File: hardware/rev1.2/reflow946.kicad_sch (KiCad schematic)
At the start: 56 parts, among them J1 VH-2A, J2 VH-3A2, J3 VH-3A2, J4 XH-A2, J5 HDR-M-2.54_2x3, J6 TFT_1.47, J7 PROBE_BRK, J8 EXT_TC, Q1 BTA16-600BRG, Q2 MMBT3906, Q3 MMBT3906, Q4 MMBT3906, SW1 SW_Push, SW2 SW_Push, SW3 SW_Push, U1 MOC3041M, U2 ESP32-WROOM-32U, U3 MAX31855KASA, U4 AMS1117-3.3, U6 MAX31855KASA

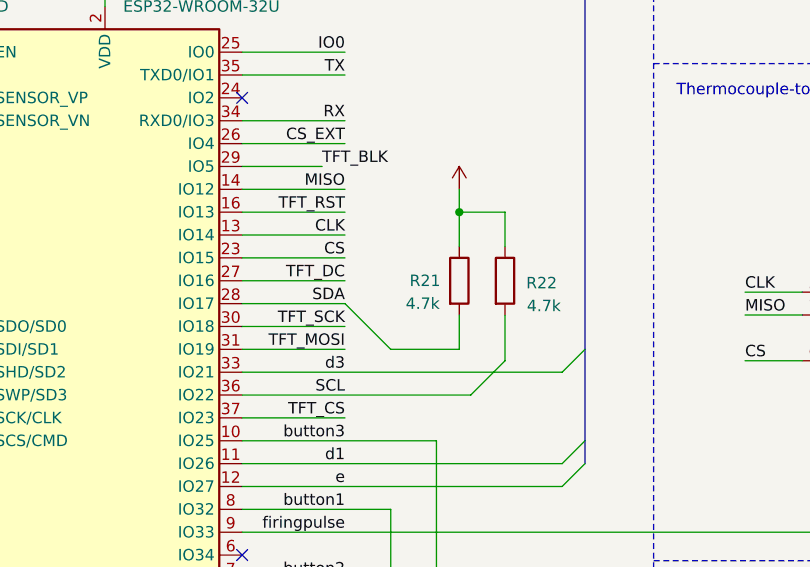
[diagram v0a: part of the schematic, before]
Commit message: rev2: remove I2C expansion pull-ups R21/R22 (vestigial — display went SPI; IO17/IO22 spare)
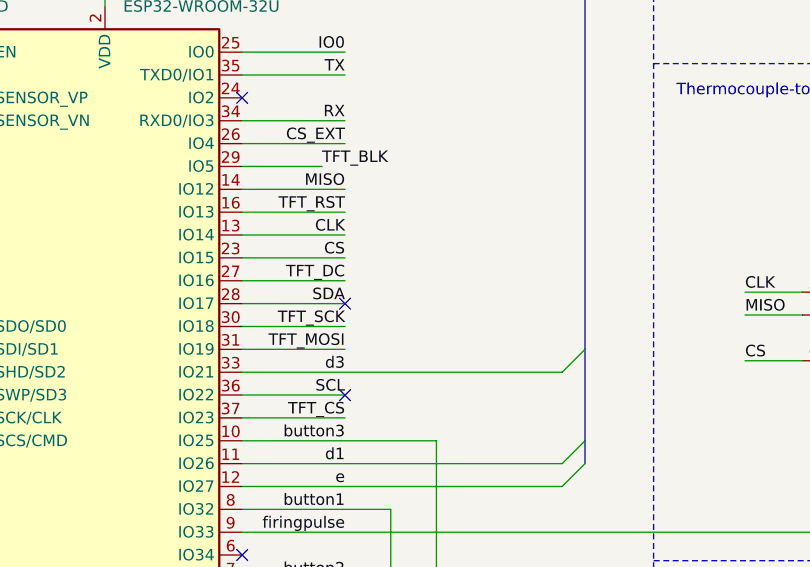
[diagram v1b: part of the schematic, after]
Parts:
- removed R21, R22: 4.7k, Resistor_SMD:R_0603_1608Metric_Pad0.98x0.95mm_HandSolder, symbol Device:R
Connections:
- no-connect marks 17 -> 19

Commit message: schematic: J6 pins reordered to FPC tail order (BL/CS/DC/RES/SDA/SCL/VDD/GND); footprint -> FH12-8S-0.5SH 0.5mm top-contact
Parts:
- J6: footprint Connector_PinHeader_2.54mm:PinHeader_1x08_P2.54mm_Vertical -> Connector_FFC-FPC:Hirose_FH12-8S-0.5SH_1x08-1MP_P0.50mm_Horizontal
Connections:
- net +3.3V: now also J6.7 (Pin_7); no longer J6.1 (Pin_1)
- net GND: now also J6.8 (Pin_8); no longer J6.2 (Pin_2)
- net TFT_BLK: now also J6.1 (Pin_1); no longer J6.8 (Pin_8)
- net TFT_CS: now also J6.2 (Pin_2); no longer J6.3 (Pin_3)
- net TFT_DC: now also J6.3 (Pin_3); no longer J6.4 (Pin_4)
- net TFT_MOSI: now also J6.5 (Pin_5); no longer J6.7 (Pin_7)
- net TFT_RST: now also J6.4 (Pin_4); no longer J6.5 (Pin_5)
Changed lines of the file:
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@@
 	(wire
 		(pts
-			(xy 181.61 223.52) (xy 176.53 223.52)
+			(xy 181.61 223.52) (xy 171.45 223.52)
 		)
 		(stroke
@@
 	(wire
 		(pts
-			(xy 171.45 236.22) (xy 181.61 236.22)
+			(xy 176.53 236.22) (xy 181.61 236.22)
 		)
 		(stroke
@@
 	(wire
 		(pts
-			(xy 181.61 220.98) (xy 176.53 220.98)
+			(xy 181.61 220.98) (xy 171.45 220.98)
 		)
 		(stroke
@@
 	(wire
 		(pts
-			(xy 171.45 238.76) (xy 181.61 238.76)
+			(xy 176.53 238.76) (xy 181.61 238.76)
 		)
 		(stroke
@@
 		)
 	)
-	(label "TFT_DC"
+	(label "TFT_RST"
 		(at 171.45 228.6 180)
 		(effects
@@
 		)
 	)
-	(label "TFT_CS"
+	(label "TFT_DC"
 		(at 171.45 226.06 180)
 		(effects
@@
 		)
 	)
-	(label "TFT_RST"
+	(label "TFT_MOSI"
 		(at 171.45 231.14 180)
 		(effects
@@
 		)
 	)
-	(label "TFT_MOSI"
-		(at 171.45 236.22 180)
-		(effects
-			(font
-				(size 1.27 1.27)
-			)
-			(justify right bottom)
-		)
-	)
 	(label "RX"
 		(at 120.65 231.14 0)
@@
 	)
 	(label "TFT_BLK"
-		(at 171.45 238.76 180)
+		(at 171.45 220.98 180)
+		(effects
+			(font
+				(size 1.27 1.27)
+			)
+			(justify right bottom)
+		)
+	)
+	(label "TFT_CS"
+		(at 171.45 223.52 180)
 		(effects
 			(font
@@
 	)
 	(symbol
+		(lib_id "power:GND")
+		(at 176.53 238.76 0)
+		(unit 1)
+		(body_style 1)
+		(exclude_from_sim no)
+		(in_bom yes)
+		(on_board yes)
+		(in_pos_files yes)
+		(dnp no)
+		(fields_autoplaced yes)
+		(property "Reference" "#PWR0126"
+			(at 176.53 242.57 0)
+			(hide yes)
+			(show_name no)
+			(do_not_autoplace no)
+			(effects
+				(font
+					(size 1.27 1.27)
+				)
+			)
+		)
+		(property "Value" "GND"
+			(at 176.53 233.67999999999998 0)
+			(hide yes)
+			(show_name no)
+			(do_not_autoplace no)
+			(effects
+				(font
+					(size 1.27 1.27)
+				)
+			)
+		)
+		(property "Footprint" ""
+			(at 176.53 238.76 0)
+			(hide yes)
+			(show_name no)
+			(do_not_autoplace no)
+			(effects
+				(font
+					(size 1.27 1.27)
+				)
+			)
+		)
+		(property "Datasheet" ""
+			(at 176.53 238.76 0)
+			(hide yes)
+			(show_name no)
+			(do_not_autoplace no)
+			(effects
+				(font
+					(size 1.27 1.27)
+				)
+			)
+		)
+		(property "Description" ""
+			(at 176.53 238.76 0)
+			(hide yes)
+			(show_name no)
+			(do_not_autoplace no)
+			(effects
+				(font
+					(size 1.27 1.27)
+				)
+			)
+		)
+		(pin "1"
+		)
+		(instances
+			(project "reflow946"
+				(path "/e06aa885-daae-4bc8-aba0-4517a19e0ae6"
+					(reference "#PWR0126")
+					(unit 1)
+				)
+			)
+		)
+	)
+	(symbol
+		(lib_id "power:+3.3V")
+		(at 176.53 236.22 0)
+		(unit 1)
+		(body_style 1)
+		(exclude_from_sim no)
+		(in_bom yes)
+		(on_board yes)
+		(in_pos_files yes)
+		(dnp no)
+		(fields_autoplaced yes)
+		(property "Reference" "#PWR0125"
+			(at 176.53 240.03 0)
+			(hide yes)
+			(show_name no)
+			(do_not_autoplace no)
+			(effects
+				(font
+					(size 1.27 1.27)
+				)
+			)
+		)
+		(property "Value" "+3.3V"
+			(at 176.53 231.14 0)
+			(hide yes)
+			(show_name no)
+			(do_not_autoplace no)
+			(effects
+				(font
+					(size 1.27 1.27)
+				)
+			)
+		)
+		(property "Footprint" ""
+			(at 176.53 236.22 0)
+			(hide yes)
+			(show_name no)
+			(do_not_autoplace no)
+			(effects
+				(font
+					(size 1.27 1.27)
+				)
+			)
+		)
+		(property "Datasheet" ""
+			(at 176.53 236.22 0)
+			(hide yes)
+			(show_name no)
+			(do_not_autoplace no)
+			(effects
+				(font
+					(size 1.27 1.27)
+				)
+			)
+		)
+		(property "Description" ""
+			(at 176.53 236.22 0)
+			(hide yes)
+			(show_name no)
+			(do_not_autoplace no)
+			(effects
+				(font
+					(size 1.27 1.27)
+				)
+			)
+		)
+		(pin "1"
+		)
+		(instances
+			(project "reflow946"
+				(path "/e06aa885-daae-4bc8-aba0-4517a19e0ae6"
+					(reference "#PWR0125")
+					(unit 1)
+				)
+			)
+		)
+	)
+	(symbol
 		(lib_id "Device:C")
 		(at 236.22 116.84 0)
@@
 	)
 	(symbol
-		(lib_id "power:+3.3V")
-		(at 176.53 220.98 0)
-		(unit 1)
-		(body_style 1)
-		(exclude_from_sim no)
-		(in_bom yes)
-		(on_board yes)
-		(in_pos_files yes)
-		(dnp no)
-		(fields_autoplaced yes)
-		(property "Reference" "#PWR0123"
-			(at 176.53 224.79 0)
-			(hide yes)
-			(show_name no)
-			(do_not_autoplace no)
-			(effects
-				(font
-					(size 1.27 1.27)
-				)
-			)
-		)
-		(property "Value" "+3.3V"
-			(at 176.53 215.9 0)
-			(hide yes)
-			(show_name no)
-			(do_not_autoplace no)
-			(effects
-				(font
-					(size 1.27 1.27)
-				)
-			)
-		)
-		(property "Footprint" ""
-			(at 176.53 220.98 0)
-			(hide yes)
-			(show_name no)
-			(do_not_autoplace no)
-			(effects
-				(font
-					(size 1.27 1.27)
-				)
-			)
-		)
-		(property "Datasheet" ""
-			(at 176.53 220.98 0)
-			(hide yes)
-			(show_name no)
-			(do_not_autoplace no)
-			(effects
-				(font
-					(size 1.27 1.27)
-				)
-			)
-		)
-		(property "Description" ""
-			(at 176.53 220.98 0)
-			(hide yes)
-			(show_name no)
-			(do_not_autoplace no)
-			(effects
-				(font
-					(size 1.27 1.27)
-				)
-			)
-		)
-		(pin "1"
-		)
-		(instances
-			(project "reflow946"
-				(path "/e06aa885-daae-4bc8-aba0-4517a19e0ae6"
-					(reference "#PWR0123")
-					(unit 1)
-				)
-			)
-		)
-	)
-	(symbol
 		(lib_id "Device:R")
 		(at 180.2866 45.72 90)
@@
 	)
 	(symbol
-		(lib_id "power:GND")
-		(at 176.53 223.52 0)
-		(unit 1)
-		(body_style 1)
-		(exclude_from_sim no)
-		(in_bom yes)
-		(on_board yes)
-		(in_pos_files yes)
-		(dnp no)
-		(fields_autoplaced yes)
-		(property "Reference" "#PWR0124"
-			(at 185.42 229.87 0)
-			(hide yes)
-			(show_name no)
-			(do_not_autoplace no)
-			(effects
-				(font
-					(size 1.27 1.27)
-				)
-			)
-		)
-		(property "Value" "GND"
-			(at 185.42 228.6 0)
-			(hide yes)
-			(show_name no)
-			(do_not_autoplace no)
-			(effects
-				(font
-					(size 1.27 1.27)
-				)
-			)
-		)
-		(property "Footprint" ""
-			(at 176.53 223.52 0)
-			(hide yes)
-			(show_name no)
-			(do_not_autoplace no)
-			(effects
-				(font
-					(size 1.27 1.27)
-				)
-			)
-		)
-		(property "Datasheet" ""
-			(at 176.53 223.52 0)
-			(hide yes)
-			(show_name no)
-			(do_not_autoplace no)
-			(effects
-				(font
-					(size 1.27 1.27)
-				)
-			)
-		)
-		(property "Description" ""
-			(at 176.53 223.52 0)
-			(hide yes)
-			(show_name no)
-			(do_not_autoplace no)
-			(effects
-				(font
-					(size 1.27 1.27)
-				)
-			)
-		)
-		(pin "1"
-		)
-		(instances
-			(project "reflow946"
-				(path "/e06aa885-daae-4bc8-aba0-4517a19e0ae6"
-					(reference "#PWR0124")
-					(unit 1)
-				)
-			)
-		)
-	)
-	(symbol
 		(lib_id "Device:R")
 		(at 152.4 161.29 0)
@@
 			)
 		)
-		(property "Footprint" "Connector_PinHeader_2.54mm:PinHeader_1x08_P2.54mm_Vertical"
+		(property "Footprint" "Connector_FFC-FPC:Hirose_FH12-8S-0.5SH_1x08-1MP_P0.50mm_Horizontal"
 			(at 186.69 220.98 0)
 			(hide yes)

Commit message: rev2: restore 7-seg plug-and-play path; dual-personality architecture complete
Schematic:
- Segment nets fully restored (a,b,c,d,f,g,dp,d2 DS1-side labels+wires;
  U2-side SDA/SCL/TFT_* reverted to segment names; NC flags removed)
- J6 pins now carry segment nets per FPC tail order:
  1=dp(BL) 2=f(CS) 3=d(DC) 4=g(RES) 5=c(SDA) 6=d2(SCL) 7=+3V3 8=GND
- Segment chain un-DNP'd (DS1, R10-R20, Q2-Q4)

Architecture: one PCB, two personalities via population —
  Board #1: DS1+segment parts fitted, FPC empty -> stock firmware, 7-seg
  Board #2: FPC+display fitted, segment parts out  -> v2 firmware, TFT
(GPIOs shared; mutually exclusive by design)

PCB:
- All pad nets synced to restored netlist (197 updated)
- Original segment routing restored from git history (62 routes)
- Stale orphan copper swept
- DRC: zero electrical violations from restoration; remaining =
  user's in-progress probe-cluster routes + unrouted new nets
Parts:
- DS1, Q3, R19: now fitted
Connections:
- net SCL is gone; now on net b: U2.36 (IO22)
- net SDA is gone; now on net a: U2.28 (IO17)
- net TFT_BLK is gone; now on net dp: J6.1 (Pin_1), U2.29 (IO5)
- net TFT_CS is gone; now on net f: J6.2 (Pin_2), U2.37 (IO23)
- net TFT_DC is gone; now on net d: J6.3 (Pin_3), U2.27 (IO16)
- net TFT_MOSI is gone; now on net c: J6.5 (Pin_5), U2.31 (IO19)
- net TFT_RST is gone; now on net g: J6.4 (Pin_4), U2.16 (IO13)
- net TFT_SCK is gone; now on net d2: J6.6 (Pin_6), U2.30 (IO18)
- net b: now reaches R15.1
- net g: now reaches R14.1
- net d2: now reaches R19.1
- net dp: now reaches R12.1
- net f: now reaches R16.1
- net a: now reaches R17.1
- net c: now reaches R13.1
- net d: now reaches R11.1
- no-connect marks 19 -> 11
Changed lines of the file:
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@@
 	)
 	(no_connect
-		(at 80.01 123.19)
-	)
-	(no_connect
-		(at 191.77 76.2)
-	)
-	(no_connect
-		(at 191.77 68.58)
-	)
-	(no_connect
 		(at 191.77 60.96)
 	)
 	(no_connect
-		(at 176.53 38.1)
-	)
-	(no_connect
-		(at 80.01 113.03)
-	)
-	(no_connect
 		(at 191.77 63.5)
 	)
 	(no_connect
-		(at 191.77 73.66)
-	)
-	(no_connect
-		(at 191.77 66.04)
-	)
-	(no_connect
 		(at 68.58 90.17)
 	)
@@
 	)
 	(no_connect
-		(at 191.77 78.74)
-	)
-	(no_connect
 		(at 38.1 92.71)
 	)
@@
 	(wire
 		(pts
-			(xy 68.58 102.87) (xy 80.01 102.87)
+			(xy 68.58 102.87) (xy 104.14 102.87)
 		)
 		(stroke
@@
 	(wire
 		(pts
-			(xy 68.58 97.79) (xy 77.47 97.79)
+			(xy 68.58 97.79) (xy 104.14 97.79)
 		)
 		(stroke
@@
 	(wire
 		(pts
-			(xy 68.58 113.03) (xy 80.01 113.03)
+			(xy 68.58 113.03) (xy 104.14 113.03)
 		)
 		(stroke
@@
 	(wire
 		(pts
-			(xy 68.58 123.19) (xy 80.01 123.19)
+			(xy 68.58 123.19) (xy 104.14 123.19)
 		)
 		(stroke
@@
 	(wire
 		(pts
-			(xy 68.58 110.49) (xy 80.01 110.49)
+			(xy 68.58 110.49) (xy 104.14 110.49)
 		)
 		(stroke
@@
 	(wire
 		(pts
-			(xy 68.58 115.57) (xy 80.01 115.57)
+			(xy 68.58 115.57) (xy 104.14 115.57)
 		)
 		(stroke
@@
 	(wire
 		(pts
-			(xy 68.58 125.73) (xy 80.01 125.73)
+			(xy 68.58 125.73) (xy 104.14 125.73)
 		)
 		(stroke
@@
 	(wire
 		(pts
-			(xy 68.58 118.11) (xy 80.01 118.11)
+			(xy 68.58 118.11) (xy 104.14 118.11)
 		)
 		(stroke
@@
 		)
 	)
-	(label "TFT_DC"
+	(label "d"
 		(at 80.01 110.49 180)
 		(effects
@@
 		)
 	)
-	(label "TFT_RST"
+	(label "g"
 		(at 171.45 228.6 180)
 		(effects
@@
 		)
 	)
-	(label "TFT_DC"
+	(label "d"
 		(at 171.45 226.06 180)
 		(effects
@@
 		)
 	)
-	(label "TFT_BLK"
+	(label "dp"
 		(at 77.47 97.79 0)
 		(effects
@@
 		)
 	)
-	(label "TFT_MOSI"
+	(label "c"
 		(at 80.01 118.11 180)
 		(effects
@@
 		)
 	)
-	(label "TFT_RST"
+	(label "g"
 		(at 80.01 102.87 180)
 		(effects
@@
 		)
 	)
-	(label "TFT_MOSI"
+	(label "c"
 		(at 171.45 231.14 180)
 		(effects
@@
 		)
 	)
-	(label "TFT_CS"
+	(label "f"
 		(at 80.01 125.73 180)
 		(effects
@@
 		)
 	)
-	(label "SDA"
+	(label "a"
 		(at 80.01 113.03 180)
 		(effects
@@
 		)
 	)
-	(label "TFT_SCK"
+	(label "d2"
 		(at 80.01 115.57 180)
 		(effects
@@
 		)
 	)
-	(label "SCL"
+	(label "b"
 		(at 80.01 123.19 180)
 		(effects
@@
 		)
 	)
-	(label "TFT_SCK"
+	(label "d2"
 		(at 171.45 233.68 180)
 		(effects
@@
 		)
 	)
-	(label "TFT_BLK"
+	(label "dp"
 		(at 171.45 220.98 180)
 		(effects
@@
 		)
 	)
-	(label "TFT_CS"
+	(label "f"
 		(at 171.45 223.52 180)
 		(effects
@@
 		)
 	)
+	(label "a"
+		(at 124.46 60.96 0)
+		(effects
+			(font
+				(size 1.27 1.27)
+			)
+			(justify left bottom)
+		)
+	)
+	(label "b"
+		(at 124.46 63.5 0)
+		(effects
+			(font
+				(size 1.27 1.27)
+			)
+			(justify left bottom)
+		)
+	)
+	(label "c"
+		(at 124.46 66.04 0)
+		(effects
+			(font
+				(size 1.27 1.27)
+			)
+			(justify left bottom)
+		)
+	)
+	(label "d"
+		(at 124.46 68.58 0)
+		(effects
+			(font
+				(size 1.27 1.27)
+			)
+			(justify left bottom)
+		)
+	)
+	(label "f"
+		(at 124.46 73.66 0)
+		(effects
+			(font
+				(size 1.27 1.27)
+			)
+			(justify left bottom)
+		)
+	)
+	(label "g"
+		(at 124.46 76.2 0)
+		(effects
+			(font
+				(size 1.27 1.27)
+			)
+			(justify left bottom)
+		)
+	)
+	(label "dp"
+		(at 124.46 78.74 0)
+		(effects
+			(font
+				(size 1.27 1.27)
+			)
+			(justify left bottom)
+		)
+	)
+	(label "d2"
+		(at 124.46 38.1 0)
+		(effects
+			(font
+				(size 1.27 1.27)
+			)
+			(justify left bottom)
+		)
+	)
+	(wire
+		(pts
+			(xy 124.46 60.96) (xy 191.77 60.96)
+		)
+		(stroke
+			(width 0)
+			(type default)
+		)
+	)
+	(wire
+		(pts
+			(xy 124.46 63.5) (xy 191.77 63.5)
+		)
+		(stroke
+			(width 0)
+			(type default)
+		)
+	)
+	(wire
+		(pts
+			(xy 124.46 66.04) (xy 191.77 66.04)
+		)
+		(stroke
+			(width 0)
+			(type default)
+		)
+	)
+	(wire
+		(pts
+			(xy 124.46 68.58) (xy 191.77 68.58)
+		)
+		(stroke
+			(width 0)
+			(type default)
+		)
+	)
+	(wire
+		(pts
+			(xy 124.46 73.66) (xy 191.77 73.66)
+		)
+		(stroke
+			(width 0)
+			(type default)
+		)
+	)
+	(wire
+		(pts
+			(xy 124.46 76.2) (xy 191.77 76.2)
+		)
+		(stroke
+			(width 0)
+			(type default)
+		)
+	)
+	(wire
+		(pts
+			(xy 124.46 78.74) (xy 191.77 78.74)
+		)
+		(stroke
+			(width 0)
+			(type default)
+		)
+	)
+	(wire
+		(pts
+			(xy 124.46 38.1) (xy 176.53 38.1)
+		)
+		(stroke
+			(width 0)
+			(type default)
+		)
+	)
 	(symbol
 		(lib_id "power:GND")
@@
 		(on_board yes)
 		(in_pos_files yes)
-		(dnp yes)
+		(dnp no)
 		(fields_autoplaced yes)
 		(property "Reference" "DS1"
@@
 		(on_board yes)
 		(in_pos_files yes)
-		(dnp yes)
+		(dnp no)
 		(property "Reference" "R19"
 			(at 180.34 33.02 90)
@@
 		(on_board yes)
 		(in_pos_files yes)
-		(dnp yes)
+		(dnp no)
 		(fields_autoplaced yes)
 		(property "Reference" "Q3"

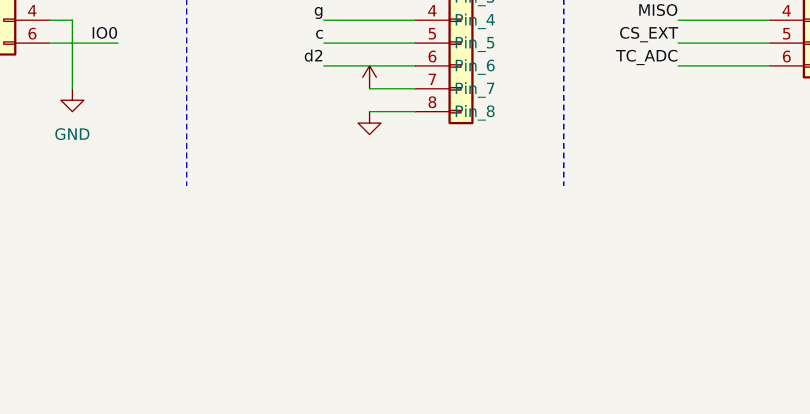
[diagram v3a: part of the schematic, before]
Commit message: rev2: add J9 2.54mm breakout header mirroring J6 FPC signals
- J9 PinHeader_1x08 @ bottom strip (142.6,124.3), same tail order:
  1=dp(BL) 2=f(CS) 3=d(DC) 4=g(RES) 5=c(SDA) 6=d2(SCL) 7=+3V3 8=GND
- Schematic: J9 symbol + label cluster cloned beside J6's
- Enables bench bring-up via pogo/dupont to standard display breakouts
  while the FH12 rehearses the v2 FPC mounting path
- Caveat: one display attached at a time (shared SPI bus)
- DRC: zero electrical violations; 16 unrouted pads remain (J6/J9 escapes)
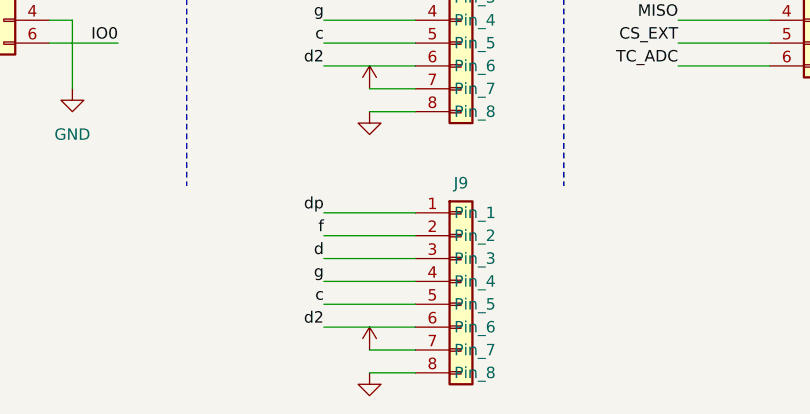
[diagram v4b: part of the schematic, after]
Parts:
- added J9: TFT_1.47, Connector_FFC-FPC:Hirose_FH12-8S-0.5SH_1x08-1MP_P0.50mm_Horizontal, symbol Connector_Generic:Conn_01x08
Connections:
- net +3.3V: now also J9.7 (Pin_7)
- net GND: now also J9.8 (Pin_8)
- net c: now also J9.5 (Pin_5)
- net d: now also J9.3 (Pin_3)
- net d2: now also J9.6 (Pin_6)
- net dp: now also J9.1 (Pin_1)
- net f: now also J9.2 (Pin_2)
- net g: now also J9.4 (Pin_4)

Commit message: manufacturing: JLC export bundle + final DRC pass
- Gerbers (7 layers), Excellon drill + map, JLC-format CPL (34 SMD,
  Y-flipped, THT stripped, DNP excluded), grouped JLC BOM (29 lines)
- DRC rule severities: silk/text/mismatch classes -> warning
- DRC final: 0 unconnected, 0 shorts/clearance/hole violations;
  remaining = silk cosmetics + baseline lib-version drift only
- BOM gap report: LCSC part numbers needed for new parts (J6/J7/J9,
  U6, C7, FB1-FB4, R6-R20 passives)
- README: interface description updated (FH12 + J9, shared-bus caveat)
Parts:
- J9: footprint Connector_FFC-FPC:Hirose_FH12-8S-0.5SH_1x08-1MP_P0.50mm_Horizontal -> Connector_PinHeader_2.54mm:PinHeader_1x08_P2.54mm_Vertical
